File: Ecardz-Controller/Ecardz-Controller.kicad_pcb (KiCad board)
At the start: 4 copper layers, 189 x 115 mm, 169 parts, among them IC1 ST25R3916B-AQWT, IC2 INA180A2IDBVR, J1 MEM2061-01-188-00-A, J10 Conn_01x02, J2 Conn_01x04, J3 Conn_01x05, J4 Conn_01x09, J5 Conn_01x01, J6 Conn_01x24, J7 Conn_01x02, J8 Conn_01x04, J9 Conn_01x04, Q1 NMOS, Q2 TMBT3904,LM, U1 STM32G0C1RETx, U2 TPS62160DSG, U3 MIC5504-3.3YM5, U4 CP2110-F02-GM1, Y1 XRCGB27M120F3M00R0

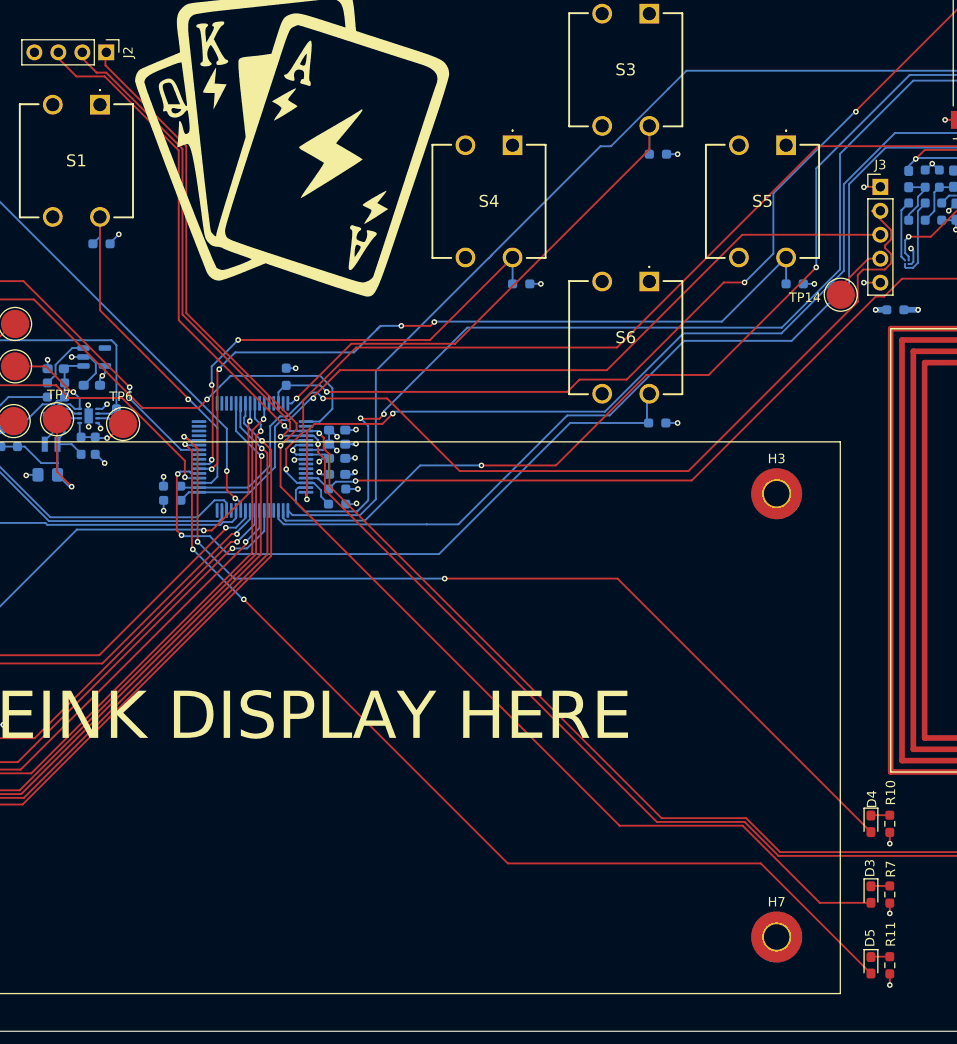
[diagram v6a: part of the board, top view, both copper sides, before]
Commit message: slightly adjusted LED position
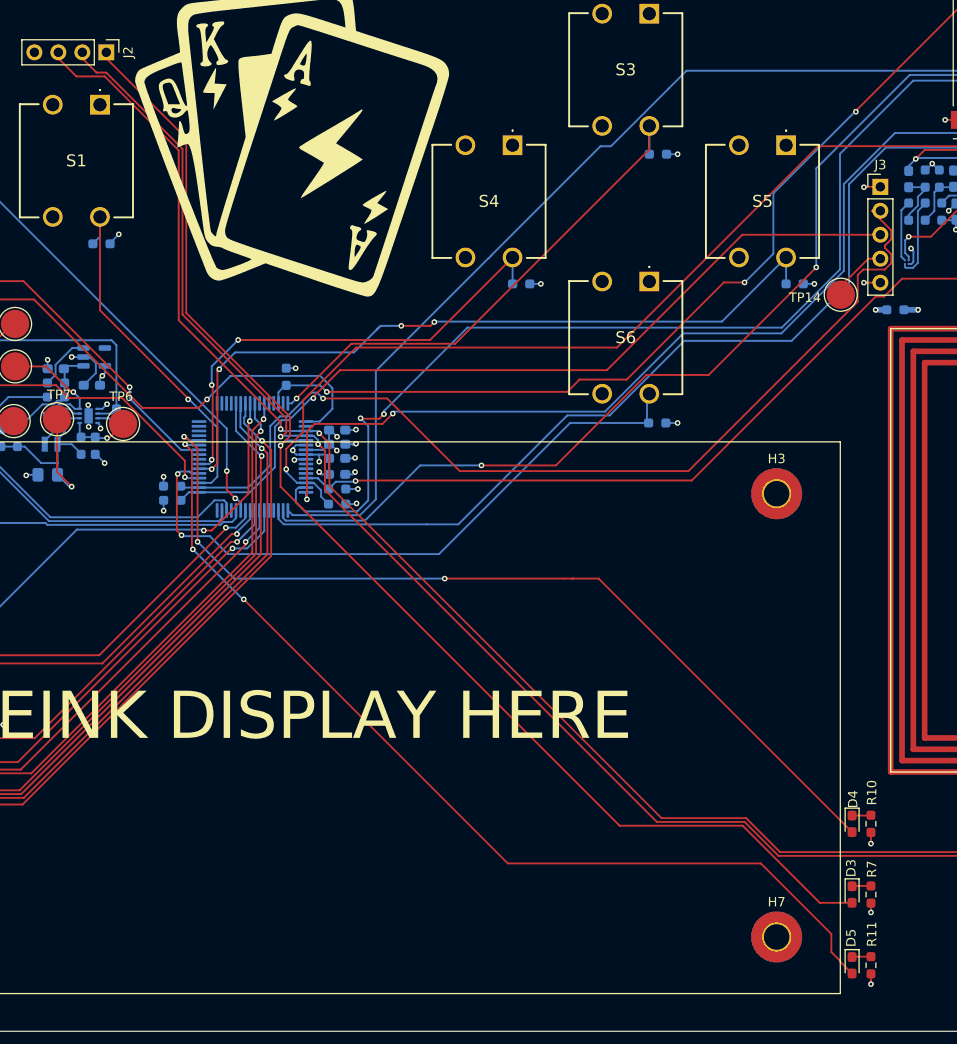
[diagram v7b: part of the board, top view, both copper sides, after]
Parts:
- moved D3 2.00 mm to (184.0, 190.5)
- moved D4 2.00 mm to (184.0, 183.0)
- moved D5 2.00 mm to (184.0, 198.0)
- moved R10 2.00 mm to (186.0, 183.0)
- moved R11 2.00 mm to (186.0, 198.0)
- moved R7 2.00 mm to (186.0, 190.5)
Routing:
- net /MCU/LED_DEBUG_B: track 139.5 -> 136.9 mm
- net /MCU/LED_DISPLAY_B: track 97.7 -> 95.8 mm
- net /MCU/LED_DISPLAY_R: track 103.5 -> 102.7 mm
